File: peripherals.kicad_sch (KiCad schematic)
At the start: 8 parts, among them J2 Conn_01x02_Socket, J3 Conn_01x04_Socket, J4 Conn_02x10

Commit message: Schematic + Layout Review Ready First Rev
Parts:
- R3: footprint (none) -> Resistor_SMD:R_0805_2012Metric_Pad1.20x1.40mm_HandSolder
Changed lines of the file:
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@@
 			)
 		)
-		(property "Footprint" ""
+		(property "Footprint" "Resistor_SMD:R_0805_2012Metric_Pad1.20x1.40mm_HandSolder"
 			(at 228.6 118.11 0)
 			(effects

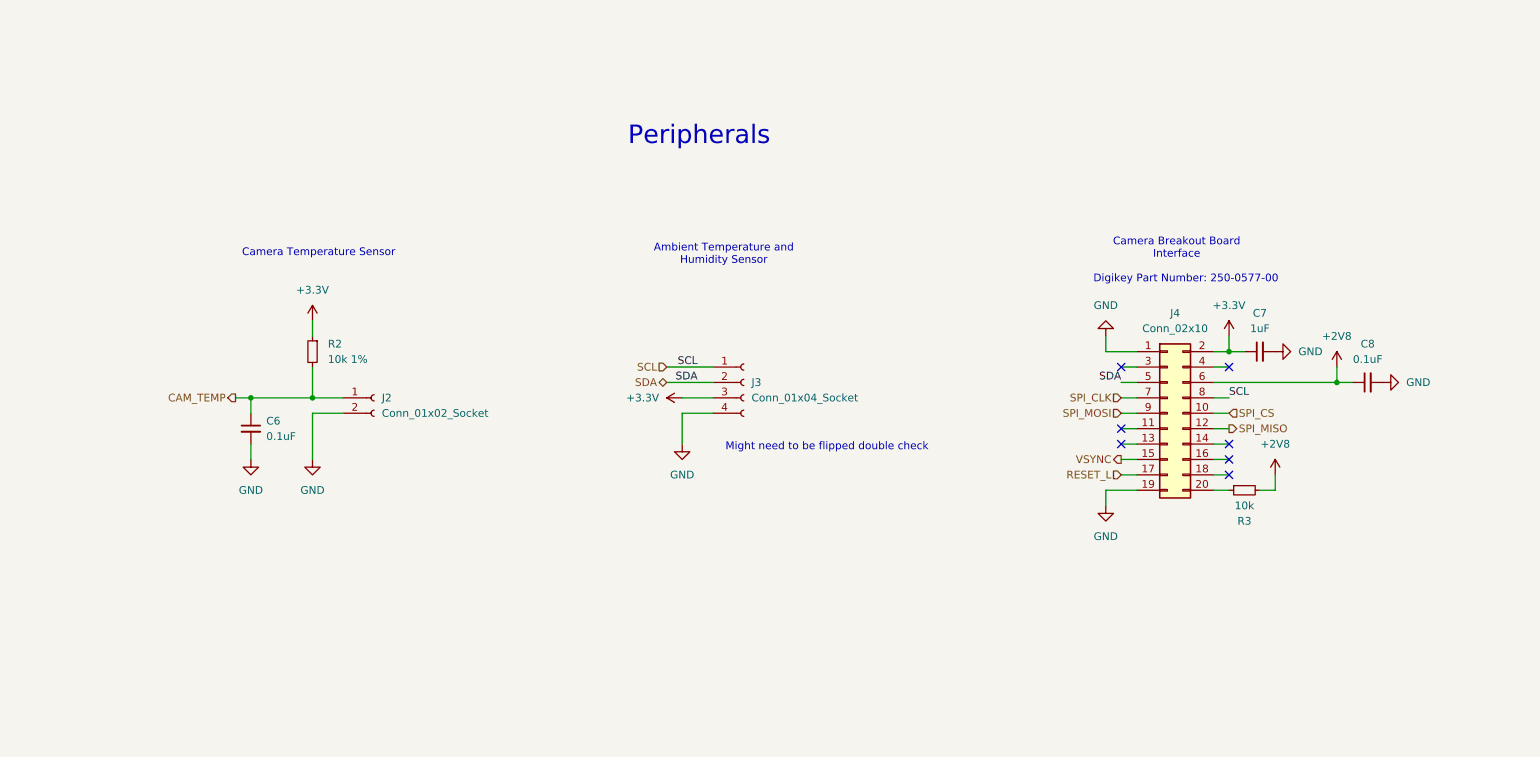
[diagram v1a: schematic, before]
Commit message: rev 2 added usb prog and i2c level shifting
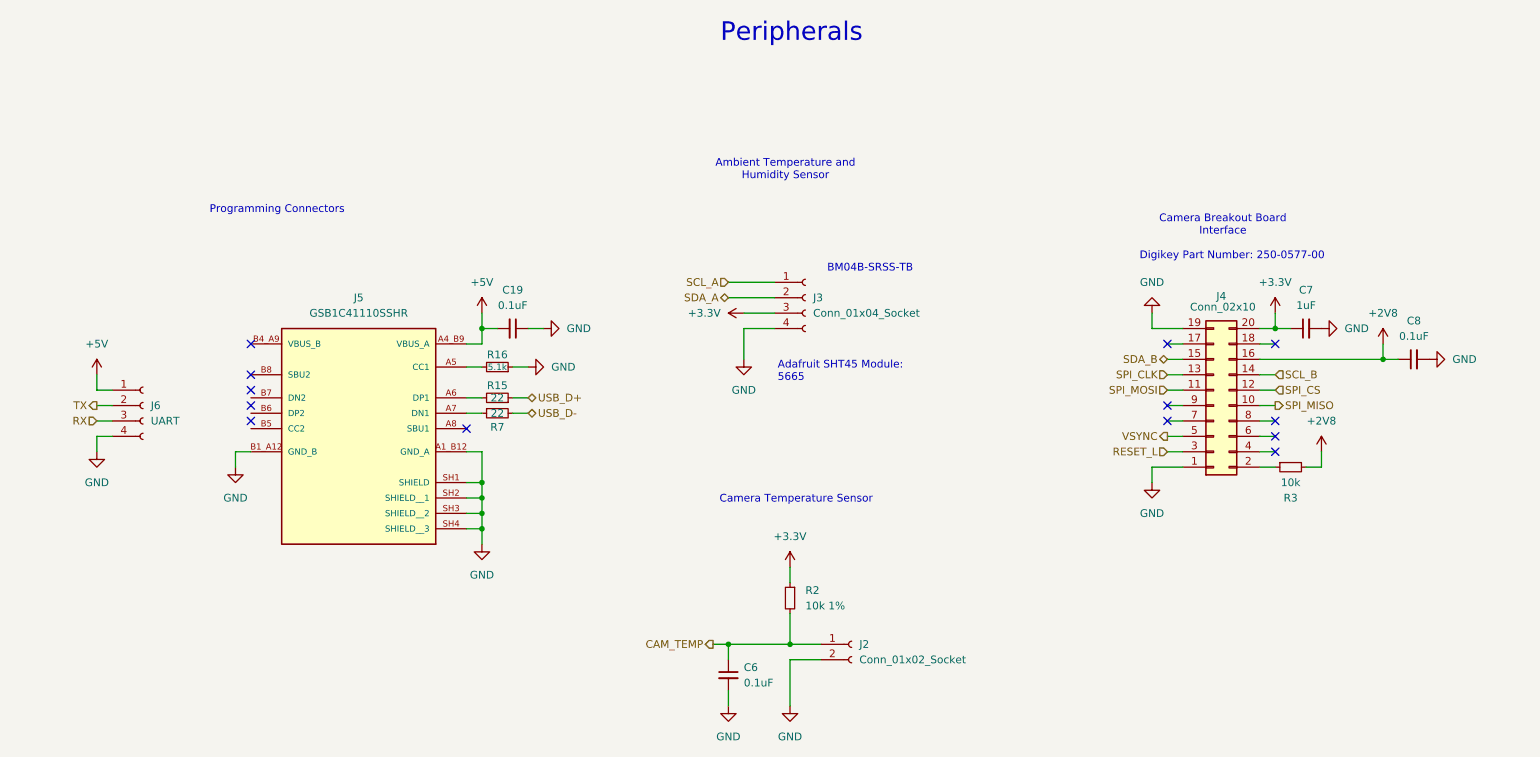
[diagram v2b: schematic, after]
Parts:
- added C19: 0.1uF, Capacitor_SMD:C_0805_2012Metric_Pad1.18x1.45mm_HandSolder, symbol Device:C_Small
- added J5: GSB1C41110SSHR, footprints:AMPHENOL_GSB1C41110SSHR, symbol GSB1C41110SSHR:GSB1C41110SSHR
- added J6: UART, footprints:CONN4_BM04B-SRSS_JST, symbol Connector:Conn_01x04_Socket
- added R15, R7: 22, Resistor_SMD:R_0805_2012Metric_Pad1.20x1.40mm_HandSolder, symbol Device:R_Small
- added R16: 5.1k, Resistor_SMD:R_0805_2012Metric_Pad1.20x1.40mm_HandSolder, symbol Device:R_Small
- J3: footprint Connector_JST:JST_SH_BM04B-SRSS-TB_1x04-1MP_P1.00mm_Vertical -> footprints:CONN4_BM04B-SRSS_JST
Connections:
- net +2V8: now also J4.16 (Pin_16); no longer J4.6 (Pin_6)
- net +3.3V: now also J4.20 (Pin_20); no longer J4.2 (Pin_2)
- net GND: now also C19.1, J5.A1_B12 (GND_A), J5.B1_A12 (GND_B), J5.SH1 (SHIELD), J5.SH2 (SHIELD__1), J5.SH3 (SHIELD__2), J5.SH4 (SHIELD__3), J6.4 (Pin_4), R16.1
- net RESET_L: now also J4.3 (Pin_3); no longer J4.17 (Pin_17)
- net SPI_CLK: now also J4.13 (Pin_13); no longer J4.7 (Pin_7)
- net SPI_CS: now also J4.12 (Pin_12); no longer J4.10 (Pin_10)
- net SPI_MISO: now also J4.10 (Pin_10); no longer J4.12 (Pin_12)
- net SPI_MOSI: now also J4.11 (Pin_11); no longer J4.9 (Pin_9)
- net VSYNC: now also J4.5 (Pin_5); no longer J4.15 (Pin_15)
- net at R3.1: now also J4.2 (Pin_2); no longer J4.20 (Pin_20)
- net SCL_B: now reaches J4.14 (Pin_14)
- net SCL: no longer names the net of J4.8 (Pin_8)
- net SCL: no longer J3.1 (Pin_1)
- net SDA renamed SDA_A
- net SDA_A: no longer J4.5 (Pin_5)
- new net: J5.A5 (CC1), R16.2
- new net: J5.A6 (DP1), R15.2
- new net: J5.A7 (DN1), R7.1
- new net +5V: C19.2, J5.A4_B9 (VBUS_A), J6.1 (Pin_1)
- new net RX: J6.3 (Pin_3)
- new net SCL_A: J3.1 (Pin_1)
- new net SDA_B: J4.15 (Pin_15)
- new net TX: J6.2 (Pin_2)
- new net USB_D+: R15.1
- new net USB_D-: R7.2
- no-connect marks 7 -> 13
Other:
- note added: "Adafruit SHT45 Module: 5665"
- note added: "BM04B-SRSS-TB"
- note added: "Programming Connectors"
- note removed: "Might need to be flipped double check"
- moved on the sheet: C6, C7, C8, J2, J3, J4, R2, R3

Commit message: minor fixes and updated PCB layout
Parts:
- renumbered J6 to J5, J5 to J6
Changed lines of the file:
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@@
 		(dnp no)
 		(fields_autoplaced yes)
-		(property "Reference" "J5"
+		(property "Reference" "J6"
 			(at 82.55 86.36 0)
 			(effects
@@
 			(project ""
 				(path "/1b613237-19dc-4add-b759-22dbb1a2d9dd/330aee13-51bd-45e1-a1f3-b7f9df002247"
-					(reference "J5")
+					(reference "J6")
 					(unit 1)
 				)
@@
 		(dnp no)
 		(fields_autoplaced yes)
-		(property "Reference" "J6"
+		(property "Reference" "J5"
 			(at 48.26 104.1399 0)
 			(effects
@@
 			(project "FrostByte_IRCamera_PCB"
 				(path "/1b613237-19dc-4add-b759-22dbb1a2d9dd/330aee13-51bd-45e1-a1f3-b7f9df002247"
-					(reference "J6")
-					(unit 1)
-				)
+					(reference "J5")
+					(unit 1)
+				)

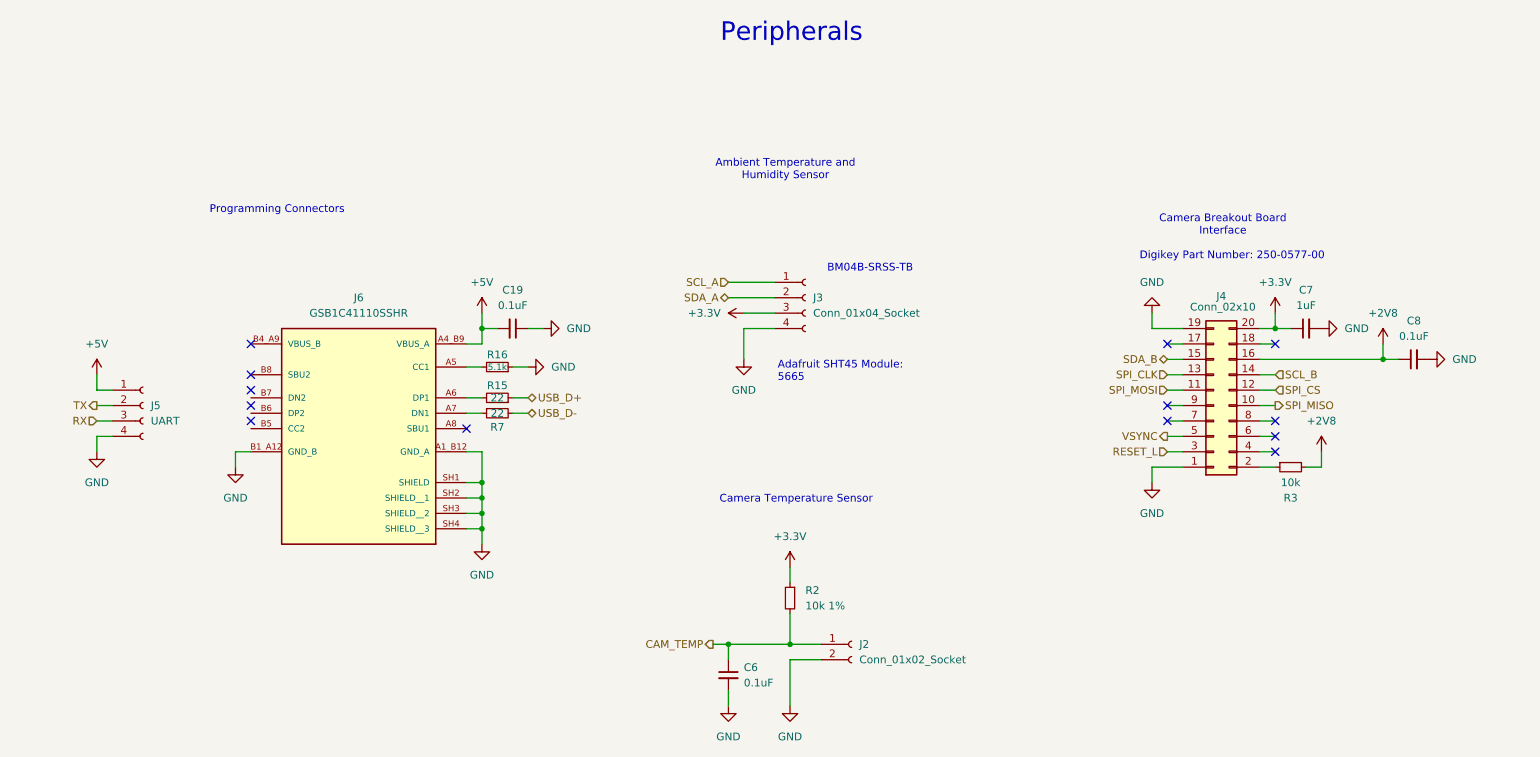
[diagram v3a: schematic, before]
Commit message: Updated Schematic and fixed some routing issues
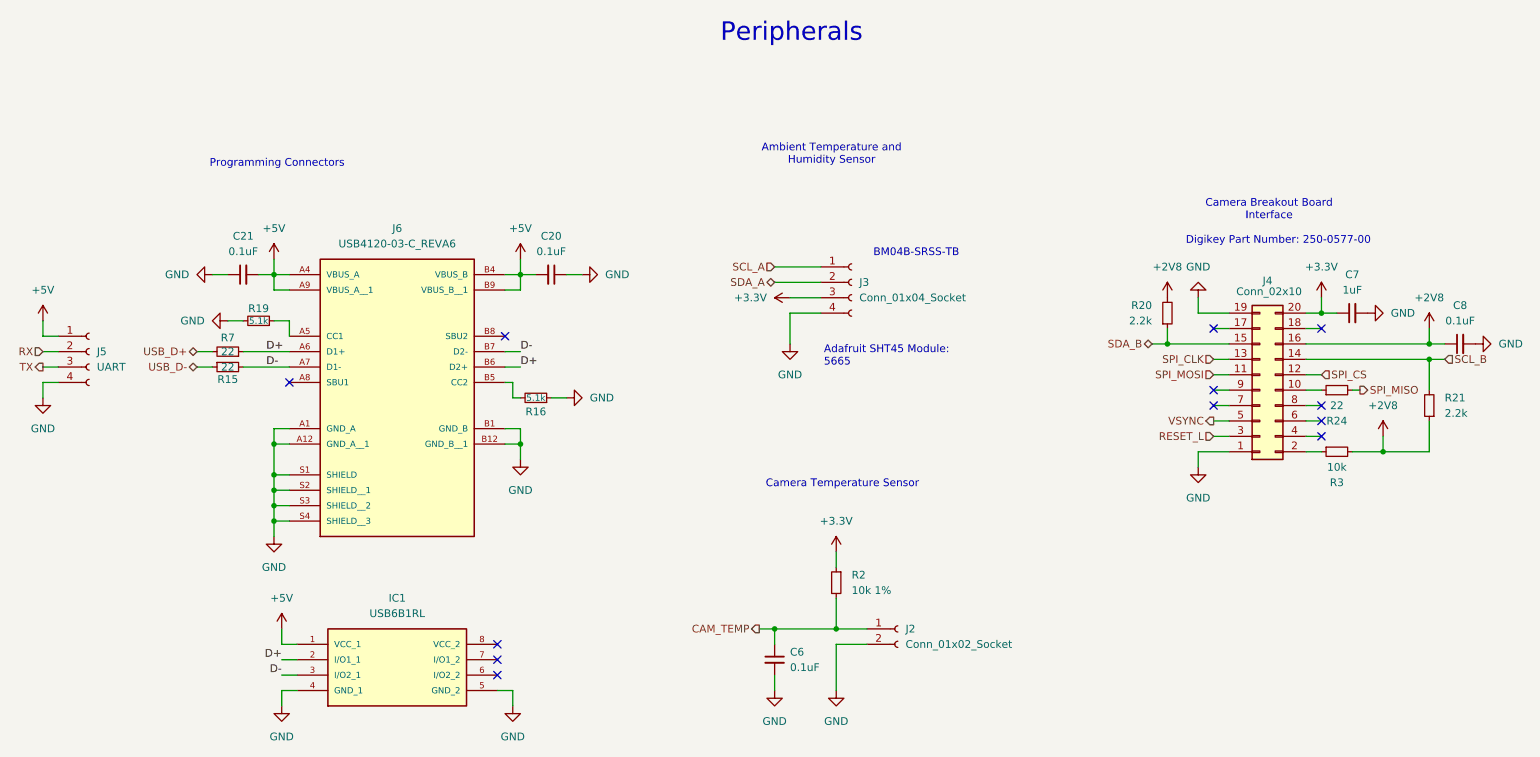
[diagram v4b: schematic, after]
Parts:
- removed C19: 0.1uF, Capacitor_SMD:C_0805_2012Metric_Pad1.18x1.45mm_HandSolder, symbol Device:C_Small
- removed J6: GSB1C41110SSHR, footprints:AMPHENOL_GSB1C41110SSHR, symbol GSB1C41110SSHR:GSB1C41110SSHR
- added C20, C21: 0.1uF, Capacitor_SMD:C_0805_2012Metric_Pad1.18x1.45mm_HandSolder, symbol Device:C_Small
- added IC1: USB6B1RL, footprints:SOIC127P600X175-8N, symbol USB6B1RL:USB6B1RL
- added J6: USB4120-03-C_REVA6, footprints:GCT_USB4120-03-C_REVA6, symbol USB4120-03-C_REVA6:USB4120-03-C_REVA6
- added R19: 5.1k, Resistor_SMD:R_0805_2012Metric_Pad1.20x1.40mm_HandSolder, symbol Device:R_Small
- added R20, R21: 2.2k, Resistor_SMD:R_0805_2012Metric_Pad1.20x1.40mm_HandSolder, symbol Device:R_Small
- added R24: 22, Resistor_SMD:R_0805_2012Metric_Pad1.20x1.40mm_HandSolder, symbol Device:R_Small
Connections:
- net +2V8: now also R20.2, R21.1
- net +5V: now also C20.2, C21.2, IC1.1 (VCC_1), J6.A4 (VBUS_A), J6.A9 (VBUS_A__1), J6.B4 (VBUS_B), J6.B9 (VBUS_B__1)
- net GND: now also C20.1, C21.1, IC1.4 (GND_1), IC1.5 (GND_2), J6.A1 (GND_A), J6.A12 (GND_A__1), J6.B1 (GND_B), J6.B12 (GND_B__1), J6.S1 (SHIELD), J6.S2 (SHIELD__1), J6.S3 (SHIELD__2), J6.S4 (SHIELD__3), R19.2
- net RX: now also J5.2 (Pin_2); no longer J5.3 (Pin_3)
- net SCL_B: now also R21.2
- net SDA_B: now also R20.1
- net SPI_MISO: now also R24.2; no longer J4.10 (Pin_10)
- net TX: now also J5.3 (Pin_3); no longer J5.2 (Pin_2)
- net USB_D+: now also R7.2; no longer R15.1
- net USB_D-: now also R15.1; no longer R7.2
- net at R16.2: now also J6.B5 (CC2)
- net D-: now reaches R15.2
- net D-: now also IC1.3 (I/O2_1), J6.A7 (D1-), J6.B7 (D2-)
- net D+: now reaches R7.1
- net D+: now also IC1.2 (I/O1_1), J6.A6 (D1+), J6.B6 (D2+)
- new net: J4.10 (Pin_10), R24.1
- new net: J6.A5 (CC1), R19.1
- no-connect marks 13 -> 12
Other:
- moved on the sheet: C6, C7, C8, J2, J3, J4, J5, R15, R16, R2, R3, R7

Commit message: Layout + Schem complete, rough routing
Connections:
- net D+ is gone; now on net USB_D+: IC1.2 (I/O1_1), J6.A6 (D1+), J6.B6 (D2+), R7.1
- net D- is gone; now on net USB_D-: IC1.3 (I/O2_1), J6.A7 (D1-), J6.B7 (D2-), R15.2
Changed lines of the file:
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@@
 		)
 	)
-	(label "D-"
-		(at 67.31 97.79 0)
+	(label "USB_D-"
+		(at 64.77 97.79 0)
 		(fields_autoplaced yes)
 		(effects
@@
 		)
 	)
-	(label "D-"
+	(label "USB_D-"
 		(at 109.22 95.25 0)
 		(fields_autoplaced yes)
@@
 		)
 	)
-	(label "D+"
+	(label "USB_D+"
 		(at 109.22 97.79 0)
 		(fields_autoplaced yes)
@@
 		)
 	)
-	(label "D-"
-		(at 69.85 148.59 180)
+	(label "USB_D+"
+		(at 69.85 146.05 180)
 		(fields_autoplaced yes)
 		(effects
@@
 		)
 	)
-	(label "D+"
-		(at 67.31 95.25 0)
+	(label "USB_D+"
+		(at 64.77 95.25 0)
 		(fields_autoplaced yes)
 		(effects
@@
 		)
 	)
-	(label "D+"
-		(at 69.85 146.05 180)
+	(label "USB_D-"
+		(at 69.85 148.59 180)
 		(fields_autoplaced yes)
 		(effects

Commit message: Rev A PCB Ordered
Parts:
- removed R20, R21: 2.2k, Resistor_SMD:R_0805_2012Metric_Pad1.20x1.40mm_HandSolder, symbol Device:R_Small
- renumbered IC1 to U5
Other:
- note added: "Programming Circuitry"
- note removed: "Peripherals"
- note removed: "Programming Connectors"
- company: (none) -> FrostByte Solutions
- title: (none) -> FrostByte IR Camera Interface Board
- moved on the sheet: C20, C21, C6, C7, C8, J2, J3, J4, J5, J6, R15, R16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
